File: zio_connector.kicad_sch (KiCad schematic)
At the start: 4 parts, among them CN10 Conn_02x17_Odd_Even, CN7 Conn_02x10_Odd_Even, CN8 Conn_02x08_Odd_Even, CN9 Conn_02x15_Odd_Even

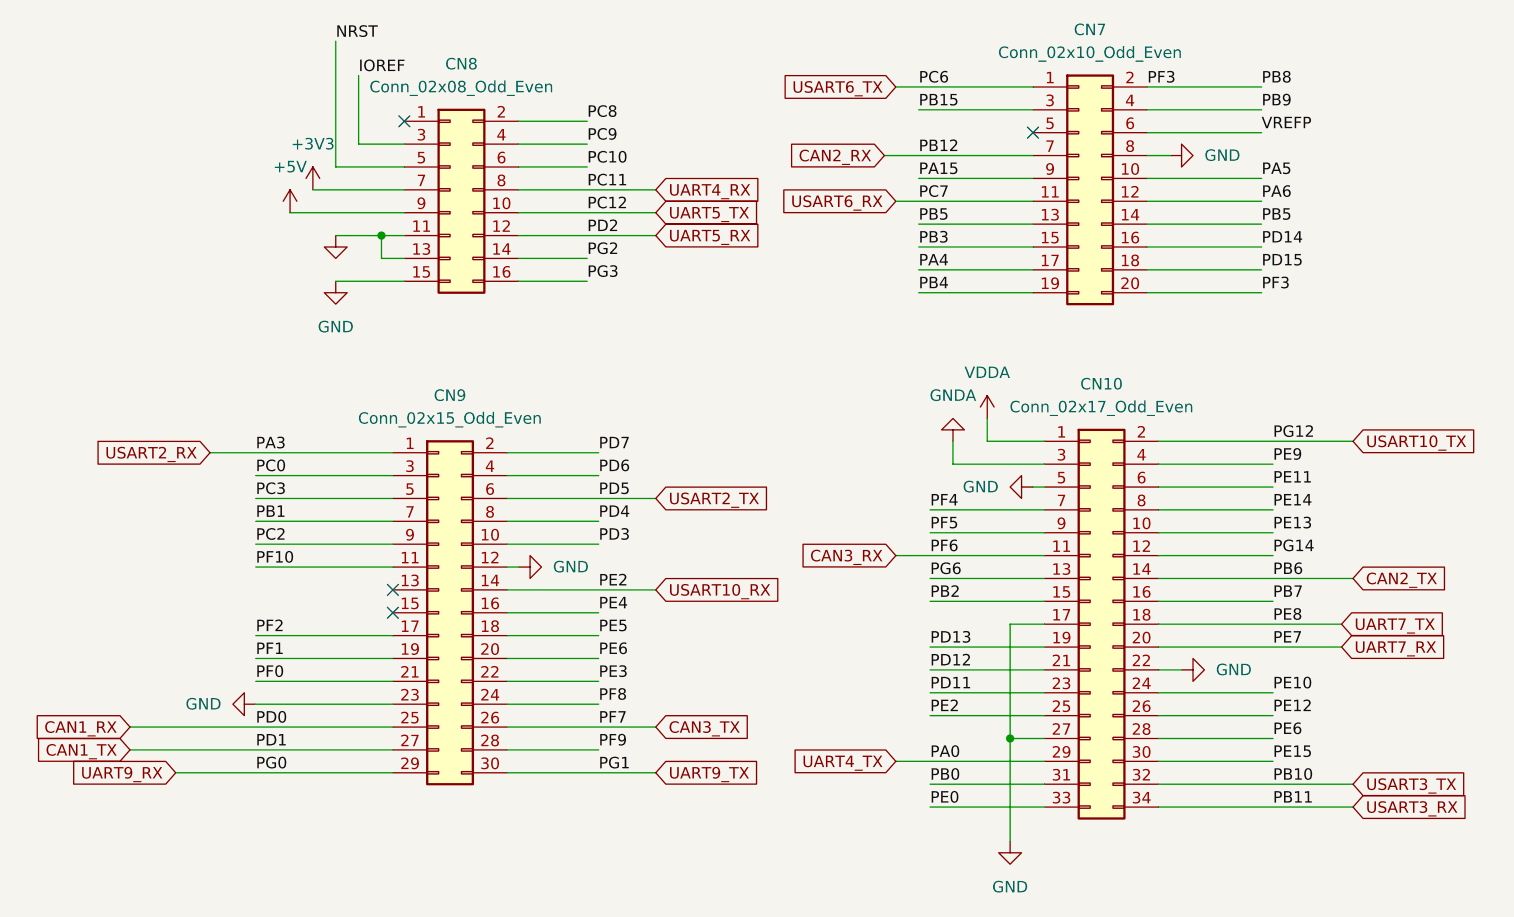
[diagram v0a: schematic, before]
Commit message: add CAN STB pins
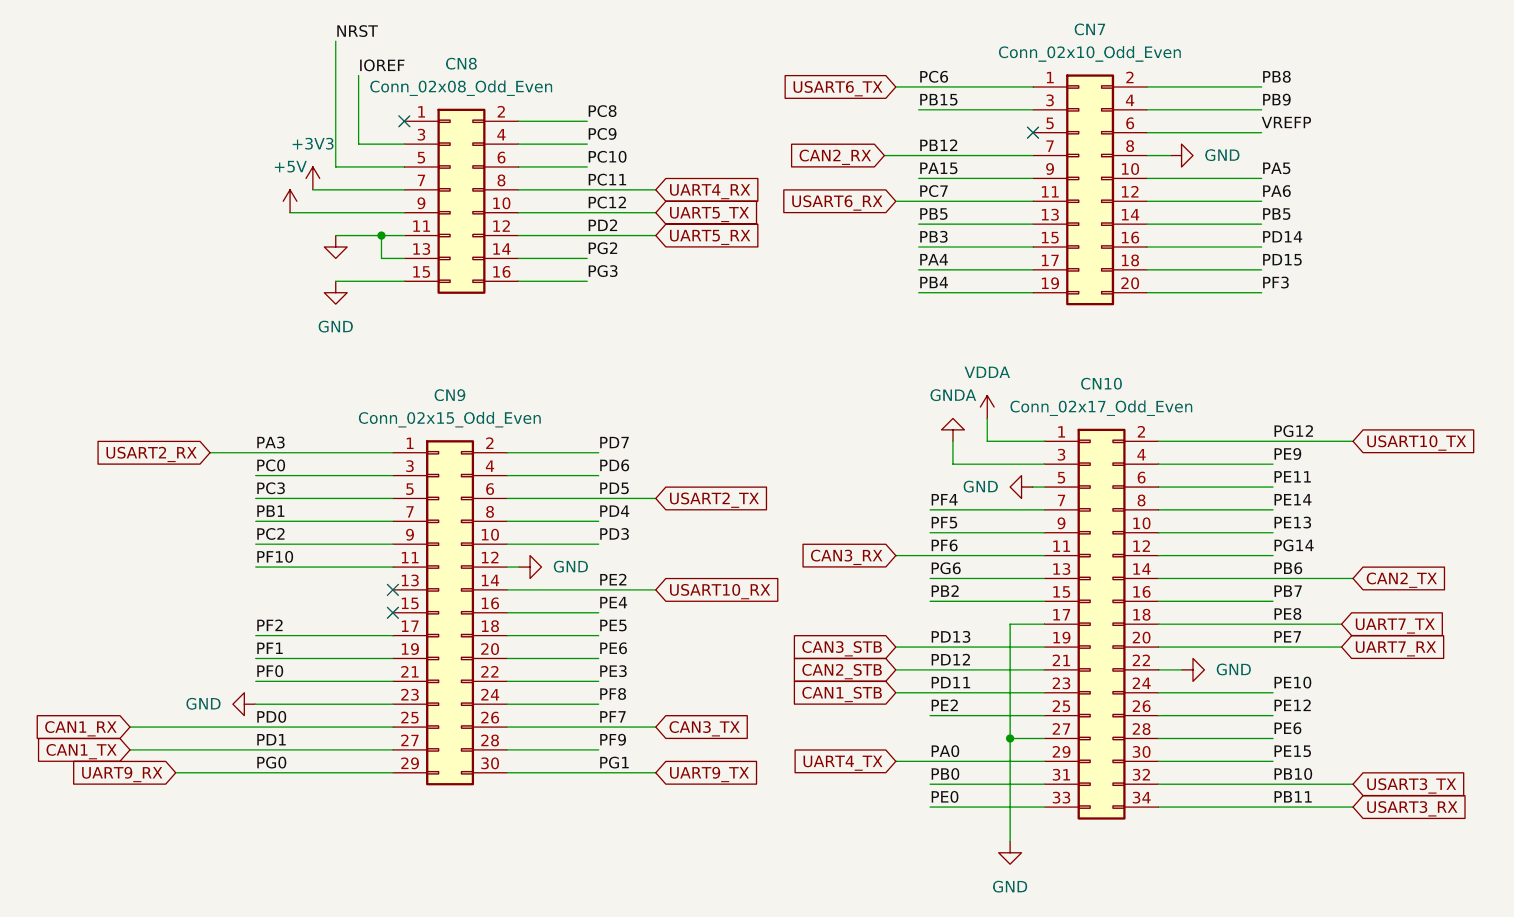
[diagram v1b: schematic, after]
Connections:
- net PB8: no longer CN7.20 (Pin_20)
- net PD11 renamed CAN1_STB
- net PD12 renamed CAN2_STB
- net PD13 renamed CAN3_STB
- new net PF3: CN7.20 (Pin_20)
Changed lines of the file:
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@@
-	(wire
-		(pts
-			(xy 120.65 87.63) (xy 133.35 87.63)
-		)
-		(stroke
-			(width 0)
-			(type default)
-		)
-	)
 	(wire
 		(pts
@@
 	(wire
 		(pts
+			(xy 116.84 87.63) (xy 133.35 87.63)
+		)
+		(stroke
+			(width 0)
+			(type default)
+		)
+	)
+	(wire
+		(pts
 			(xy 73.66 81.28) (xy 90.17 81.28)
 		)
@@
 	(wire
 		(pts
-			(xy 133.35 90.17) (xy 120.65 90.17)
-		)
-		(stroke
-			(width 0)
-			(type default)
-		)
-	)
-	(wire
-		(pts
 			(xy 45.72 71.12) (xy 60.96 71.12)
 		)
@@
 	(wire
 		(pts
-			(xy 120.65 92.71) (xy 133.35 92.71)
-		)
-		(stroke
-			(width 0)
-			(type default)
-		)
-	)
-	(wire
-		(pts
 			(xy 119.38 27.94) (xy 132.08 27.94)
 		)
@@
 	(wire
 		(pts
+			(xy 116.84 92.71) (xy 133.35 92.71)
+		)
+		(stroke
+			(width 0)
+			(type default)
+		)
+	)
+	(wire
+		(pts
 			(xy 132.08 69.85) (xy 133.35 69.85)
 		)
@@
 		(pts
 			(xy 144.78 40.64) (xy 157.48 40.64)
+		)
+		(stroke
+			(width 0)
+			(type default)
+		)
+	)
+	(wire
+		(pts
+			(xy 116.84 90.17) (xy 133.35 90.17)
 		)
 		(stroke
@@
 	(label "PC10"
 		(at 82.55 34.29 0)
-		(fields_autoplaced yes)
-		(effects
-			(font
-				(size 1.27 1.27)
-			)
-			(justify left bottom)
-		)
-	)
-	(label "PF3"
-		(at 144.78 25.4 0)
 		(fields_autoplaced yes)
 		(effects
@@
 		)
 	)
+	(global_label "CAN1_STB"
+		(shape input)
+		(at 116.84 92.71 180)
+		(fields_autoplaced yes)
+		(effects
+			(font
+				(size 1.27 1.27)
+			)
+			(justify right)
+		)
+		(property "Intersheetrefs" "${INTERSHEET_REFS}"
+			(at 104.5415 92.71 0)
+			(effects
+				(font
+					(size 1.27 1.27)
+				)
+				(justify right)
+				(hide yes)
+			)
+		)
+	)
 	(global_label "UART5_TX"
 		(shape input)
@@
 		)
 	)
-	(global_label "USART6_RX"
-		(shape input)
-		(at 116.84 38.1 180)
+	(global_label "CAN3_STB"
+		(shape input)
+		(at 116.84 87.63 180)
 		(fields_autoplaced yes)
 		(effects
@@
 		)
 		(property "Intersheetrefs" "${INTERSHEET_REFS}"
-			(at 103.332 38.1 0)
+			(at 104.5415 87.63 0)
 			(effects
 				(font
@@
 		)
 	)
-	(global_label "CAN2_RX"
-		(shape input)
-		(at 115.57 33.02 180)
+	(global_label "USART6_RX"
+		(shape input)
+		(at 116.84 38.1 180)
 		(fields_autoplaced yes)
 		(effects
@@
 		)
 		(property "Intersheetrefs" "${INTERSHEET_REFS}"
-			(at 104.2391 33.02 0)
+			(at 103.332 38.1 0)
 			(effects
 				(font
@@
 		)
 	)
+	(global_label "CAN2_RX"
+		(shape input)
+		(at 115.57 33.02 180)
+		(fields_autoplaced yes)
+		(effects
+			(font
+				(size 1.27 1.27)
+			)
+			(justify right)
+		)
+		(property "Intersheetrefs" "${INTERSHEET_REFS}"
+			(at 104.2391 33.02 0)
+			(effects
+				(font
+					(size 1.27 1.27)
+				)
+				(justify right)
+				(hide yes)
+			)
+		)
+	)
 	(global_label "CAN3_TX"
 		(shape input)
@@
 			(effects
 				(font
+					(size 1.27 1.27)
+				)
+				(justify right)
+				(hide yes)
+			)
+		)
+	)
+	(global_label "CAN2_STB"
+		(shape input)
+		(at 116.84 90.17 180)
+		(fields_autoplaced yes)
+		(effects
+			(font
+				(size 1.27 1.27)
+			)
+			(justify right)
+		)
+		(property "Intersheetrefs" "${INTERSHEET_REFS}"
+			(at 104.5415 90.17 0)
+			(effects
+				(font

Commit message: fix some placement
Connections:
- net GND: no longer CN8.15 (Pin_15)
- new net VIN: CN8.15 (Pin_15)

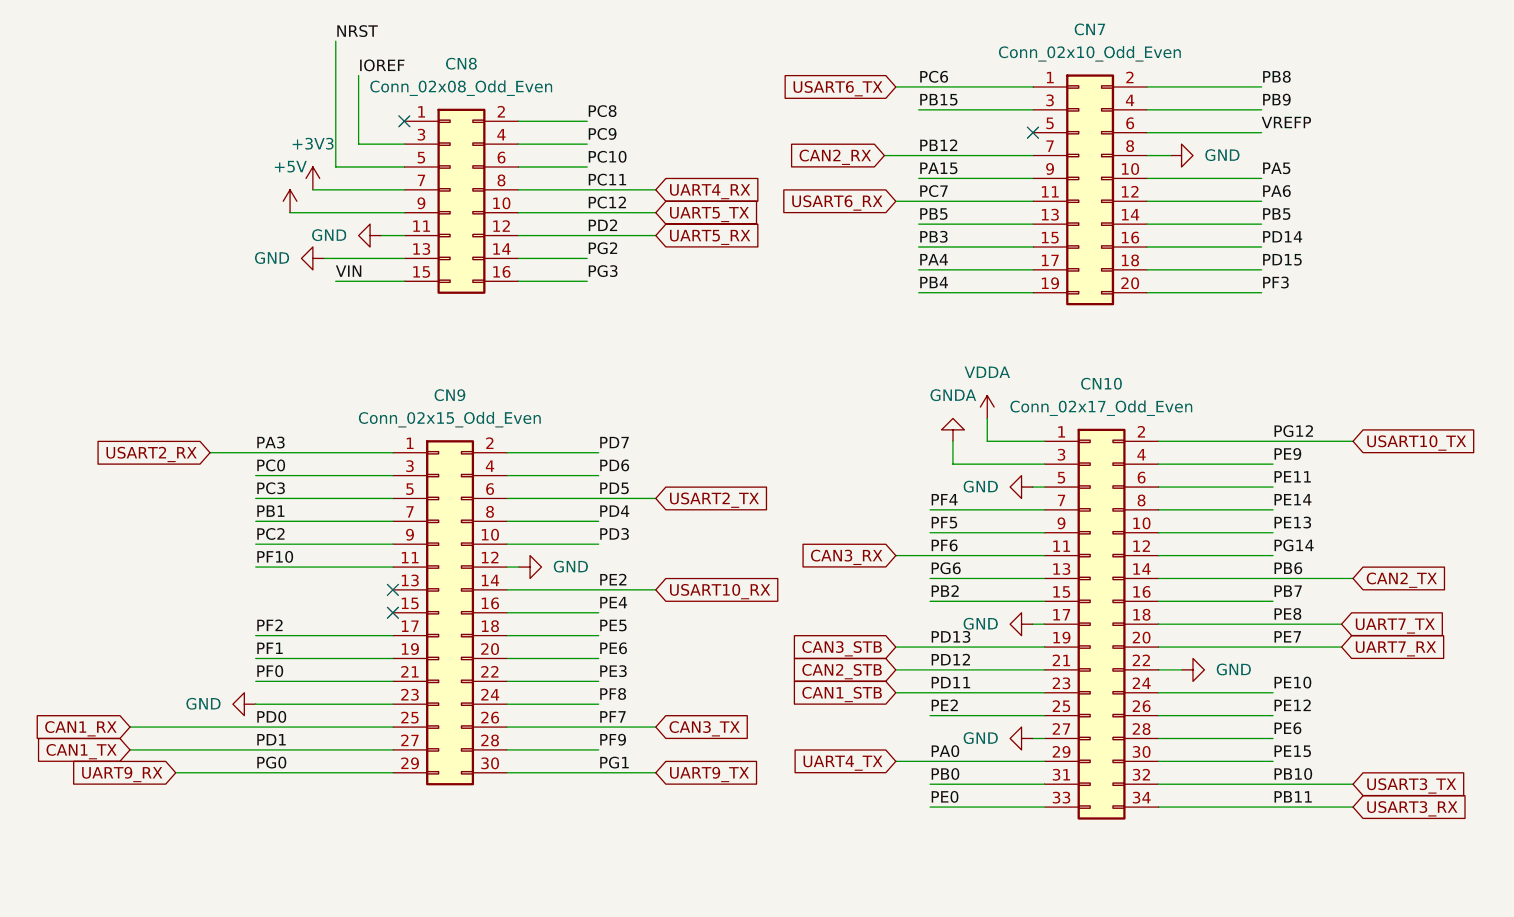
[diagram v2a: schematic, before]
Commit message: readdress CAN pins for better routing
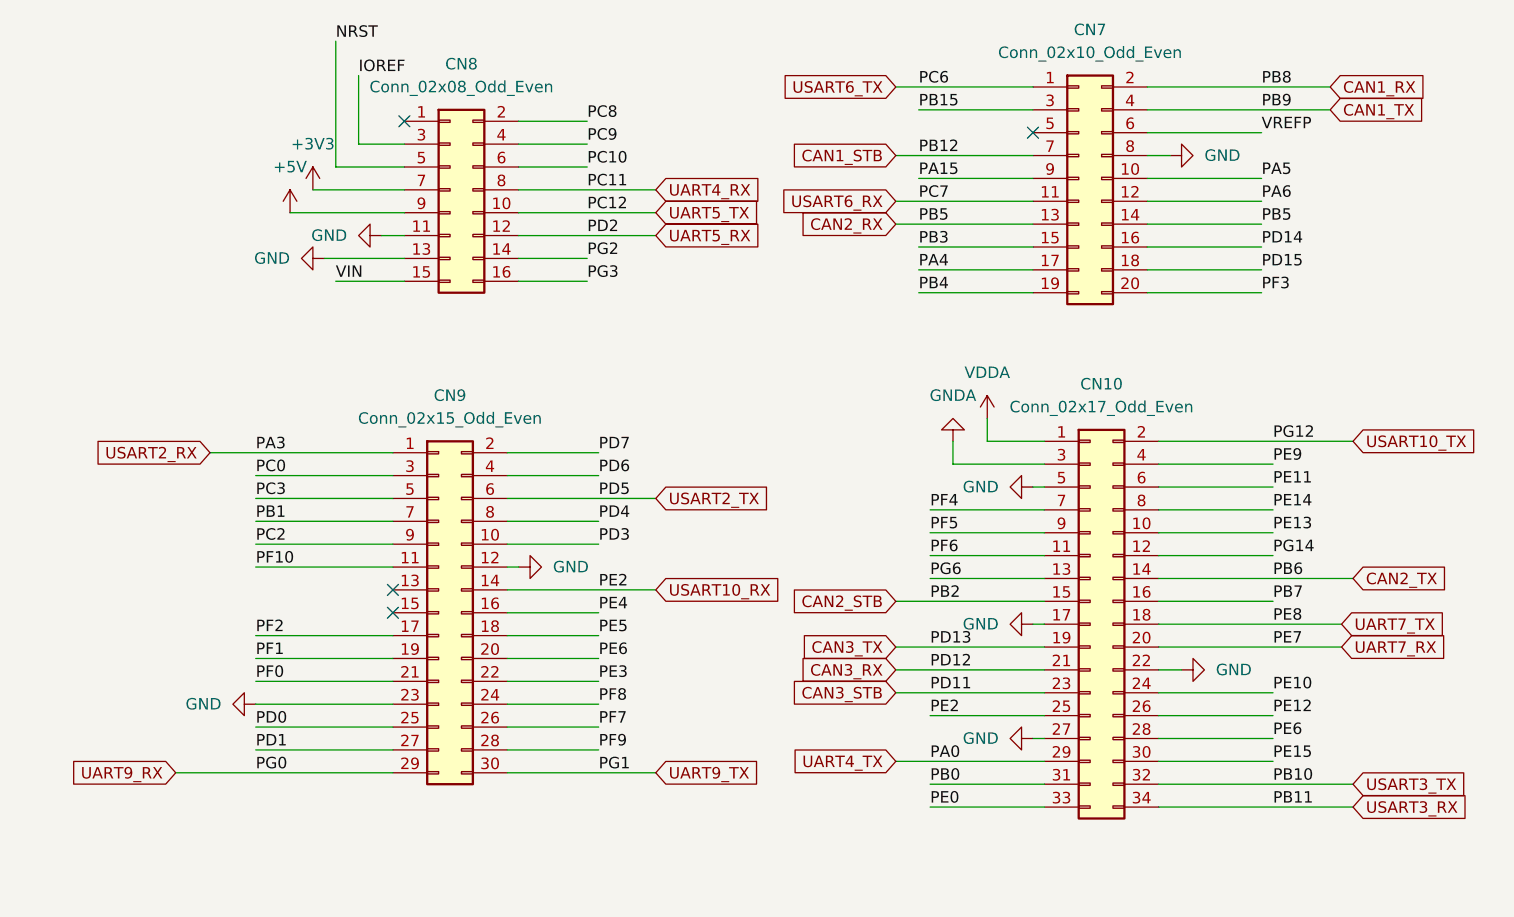
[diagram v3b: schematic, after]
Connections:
- net PB2 is gone; now on net CAN2_STB: CN10.15 (Pin_15)
- net PB5 is gone; now on net CAN2_RX: CN7.13 (Pin_13), CN7.14 (Pin_14)
- net PB8 is gone; now on net CAN1_RX: CN7.2 (Pin_2)
- net PB9 is gone; now on net CAN1_TX: CN7.4 (Pin_4)
- net CAN1_RX: no longer CN9.25 (Pin_25)
- net CAN1_STB: now also CN7.7 (Pin_7); no longer CN10.23 (Pin_23)
- net CAN1_TX: no longer CN9.27 (Pin_27)
- net CAN2_RX: no longer CN7.7 (Pin_7)
- net CAN2_STB: no longer CN10.21 (Pin_21)
- net CAN3_RX: now also CN10.21 (Pin_21); no longer CN10.11 (Pin_11)
- net CAN3_STB: now also CN10.23 (Pin_23); no longer CN10.19 (Pin_19)
- net CAN3_TX: now also CN10.19 (Pin_19); no longer CN9.26 (Pin_26)
- new net PD0: CN9.25 (Pin_25)
- new net PD1: CN9.27 (Pin_27)
- new net PF6: CN10.11 (Pin_11)
- new net PF7: CN9.26 (Pin_26)

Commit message: uarts routed
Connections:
- net PD0 is gone; now on net UART4_RX: CN9.25 (Pin_25)
- net PD1 is gone; now on net UART4_TX: CN9.27 (Pin_27)
- net PE3 is gone; now on net USART10_TX: CN9.22 (Pin_22)
- net PE6: no longer CN10.28 (Pin_28)
- net UART4_RX: no longer CN8.8 (Pin_8)
- net UART4_TX: no longer CN10.29 (Pin_29)
- net USART10_RX: no longer CN10.25 (Pin_25)
- net USART10_TX: no longer CN10.2 (Pin_2)
- new net PA0: CN10.29 (Pin_29)
- new net PC11: CN8.8 (Pin_8)
- new net PG12: CN10.2 (Pin_2)
- no-connect marks 4 -> 8
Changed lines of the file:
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@@
 	(paper "A4")
 	(no_connect
+		(at 133.35 95.25)
+	)
+	(no_connect
 		(at 132.08 30.48)
 	)
@@
 	)
 	(no_connect
+		(at 146.05 97.79)
+	)
+	(no_connect
 		(at 60.96 81.28)
 	)
@@
 		(at 60.96 83.82)
 	)
+	(no_connect
+		(at 120.65 95.25)
+	)
+	(no_connect
+		(at 158.75 97.79)
+	)
 	(wire
 		(pts
@@
 	(wire
 		(pts
+			(xy 120.65 100.33) (xy 133.35 100.33)
+		)
+		(stroke
+			(width 0)
+			(type default)
+		)
+	)
+	(wire
+		(pts
 			(xy 119.38 35.56) (xy 132.08 35.56)
 		)
@@
 	(wire
 		(pts
-			(xy 74.93 36.83) (xy 90.17 36.83)
-		)
-		(stroke
-			(width 0)
-			(type default)
-		)
-	)
-	(wire
-		(pts
 			(xy 116.84 33.02) (xy 132.08 33.02)
 		)
@@
 	(wire
 		(pts
-			(xy 45.72 99.06) (xy 60.96 99.06)
-		)
-		(stroke
-			(width 0)
-			(type default)
-		)
-	)
-	(wire
-		(pts
 			(xy 144.78 27.94) (xy 165.1 27.94)
 		)
@@
 	(wire
 		(pts
+			(xy 74.93 36.83) (xy 82.55 36.83)
+		)
+		(stroke
+			(width 0)
+			(type default)
+		)
+	)
+	(wire
+		(pts
 			(xy 144.78 45.72) (xy 157.48 45.72)
 		)
@@
 	(wire
 		(pts
-			(xy 146.05 97.79) (xy 158.75 97.79)
-		)
-		(stroke
-			(width 0)
-			(type default)
-		)
-	)
-	(wire
-		(pts
 			(xy 73.66 76.2) (xy 83.82 76.2)
 		)
@@
 	(wire
 		(pts
-			(xy 146.05 64.77) (xy 167.64 64.77)
-		)
-		(stroke
-			(width 0)
-			(type default)
-		)
-	)
-	(wire
-		(pts
 			(xy 116.84 90.17) (xy 133.35 90.17)
 		)
@@
 	(wire
 		(pts
-			(xy 45.72 96.52) (xy 60.96 96.52)
-		)
-		(stroke
-			(width 0)
-			(type default)
-		)
-	)
-	(wire
-		(pts
 			(xy 53.34 44.45) (xy 62.23 44.45)
 		)
@@
 	(wire
 		(pts
+			(xy 146.05 64.77) (xy 158.75 64.77)
+		)
+		(stroke
+			(width 0)
+			(type default)
+		)
+	)
+	(wire
+		(pts
 			(xy 116.84 82.55) (xy 133.35 82.55)
 		)
@@
 	(wire
 		(pts
-			(xy 116.84 100.33) (xy 133.35 100.33)
-		)
-		(stroke
-			(width 0)
-			(type default)
-		)
-	)
-	(wire
-		(pts
 			(xy 49.53 39.37) (xy 62.23 39.37)
 		)
@@
 	(wire
 		(pts
-			(xy 73.66 91.44) (xy 83.82 91.44)
+			(xy 36.83 96.52) (xy 60.96 96.52)
+		)
+		(stroke
+			(width 0)
+			(type default)
+		)
+	)
+	(wire
+		(pts
+			(xy 73.66 91.44) (xy 90.17 91.44)
 		)
 		(stroke
@@
 	(wire
 		(pts
-			(xy 120.65 95.25) (xy 133.35 95.25)
-		)
-		(stroke
-			(width 0)
-			(type default)
-		)
-	)
-	(wire
-		(pts
 			(xy 146.05 100.33) (xy 158.75 100.33)
 		)
@@
 		(pts
 			(xy 116.84 87.63) (xy 133.35 87.63)
+		)
+		(stroke
+			(width 0)
+			(type default)
+		)
+	)
+	(wire
+		(pts
+			(xy 36.83 99.06) (xy 60.96 99.06)
 		)
 		(stroke
@@
 	(global_label "UART4_RX"
 		(shape input)
-		(at 90.17 36.83 0)
-		(fields_autoplaced yes)
-		(effects
-			(font
-				(size 1.27 1.27)
-			)
-			(justify left)
+		(at 36.83 96.52 180)
+		(fields_autoplaced yes)
+		(effects
+			(font
+				(size 1.27 1.27)
+			)
+			(justify right)
 		)
 		(property "Intersheetrefs" "${INTERSHEET_REFS}"
-			(at 102.4685 36.83 0)
+			(at 24.5315 96.52 0)
 			(effects
 				(font
 					(size 1.27 1.27)
 				)
-				(justify left)
+				(justify right)
 				(hide yes)
 			)
@@
 	(global_label "USART10_TX"
 		(shape input)
-		(at 167.64 64.77 0)
+		(at 90.17 91.44 0)
 		(fields_autoplaced yes)
 		(effects
@@
 		)
 		(property "Intersheetrefs" "${INTERSHEET_REFS}"
-			(at 182.0551 64.77 0)
+			(at 104.5851 91.44 0)
 			(effects
 				(font
@@
 	(global_label "UART4_TX"
 		(shape input)
-		(at 116.84 100.33 180)
+		(at 36.83 99.06 180)
 		(fields_autoplaced yes)
 		(effects
@@
 		)
 		(property "Intersheetrefs" "${INTERSHEET_REFS}"
-			(at 104.8439 100.33 0)
+			(at 24.8339 99.06 0)
 			(effects
 				(font

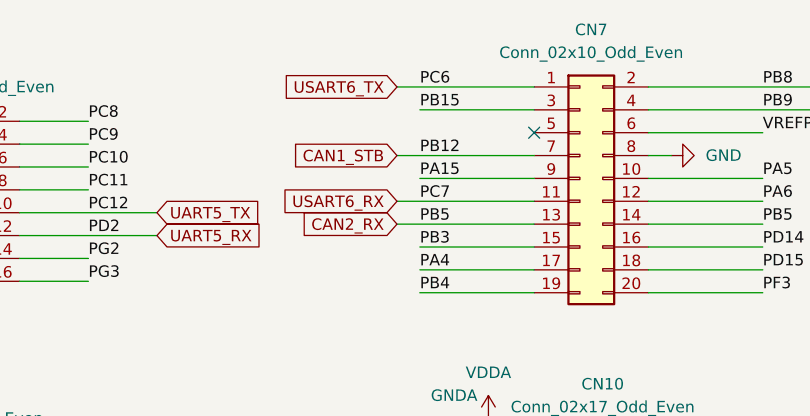
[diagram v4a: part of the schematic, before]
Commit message: some connection for CAN1
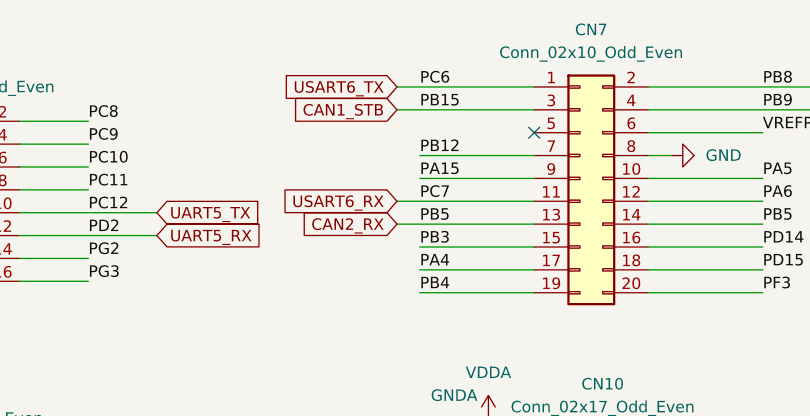
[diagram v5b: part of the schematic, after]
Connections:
- net PB15 is gone; now on net CAN1_STB: CN7.3 (Pin_3)
- net CAN1_STB: no longer CN7.7 (Pin_7)
- new net PB12: CN7.7 (Pin_7)
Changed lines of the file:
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@@
-	(wire
-		(pts
-			(xy 116.84 33.02) (xy 132.08 33.02)
-		)
-		(stroke
-			(width 0)
-			(type default)
-		)
-	)
 	(wire
 		(pts
@@
 	(wire
 		(pts
-			(xy 119.38 27.94) (xy 132.08 27.94)
+			(xy 119.38 33.02) (xy 132.08 33.02)
 		)
 		(stroke
@@
 		(pts
 			(xy 73.66 96.52) (xy 83.82 96.52)
+		)
+		(stroke
+			(width 0)
+			(type default)
+		)
+	)
+	(wire
+		(pts
+			(xy 116.84 27.94) (xy 132.08 27.94)
 		)
 		(stroke
@@
 	(global_label "CAN1_STB"
 		(shape input)
-		(at 116.84 33.02 180)
+		(at 116.84 27.94 180)
 		(fields_autoplaced yes)
 		(effects
@@
 		)
 		(property "Intersheetrefs" "${INTERSHEET_REFS}"
-			(at 104.5415 33.02 0)
+			(at 104.5415 27.94 0)
 			(effects
 				(font
